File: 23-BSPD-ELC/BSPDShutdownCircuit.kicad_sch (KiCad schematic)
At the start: 15 parts, among them Q3 Q_NMOS_GSD-Device, Q4 Q_NMOS_GSD-Device, Q5 Q_PMOS_GDS, Q6 Q_PMOS_GDS

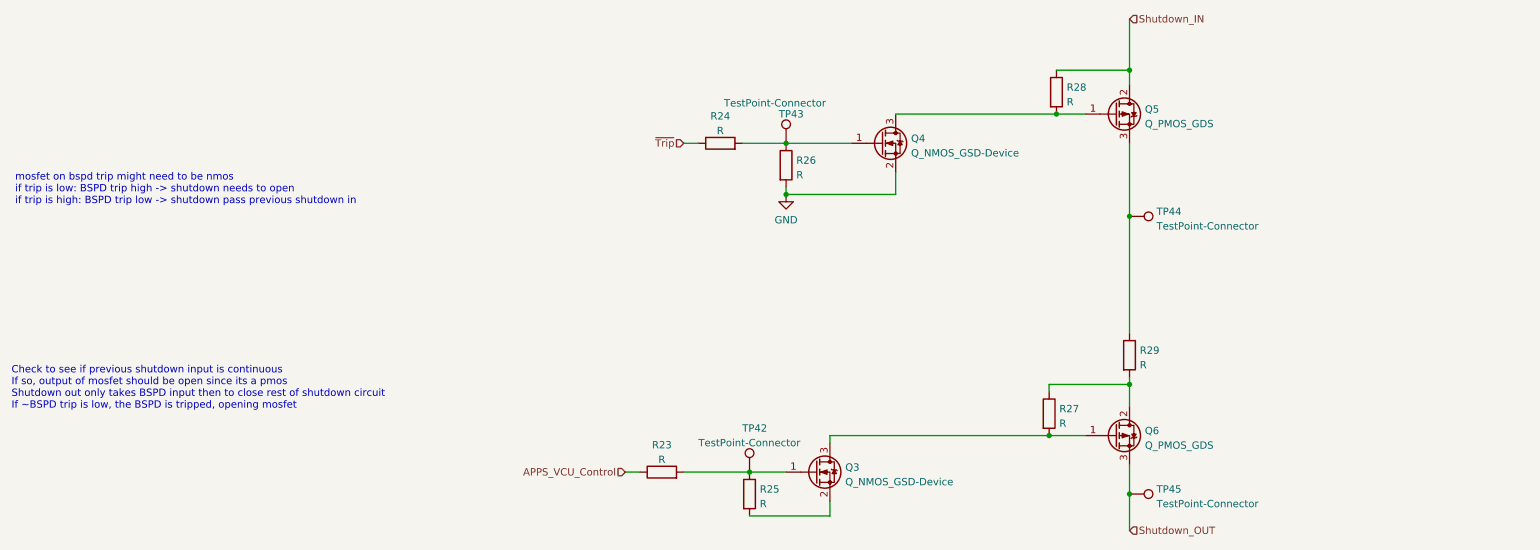
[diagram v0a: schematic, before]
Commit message: Revision changes and updates to some footprints
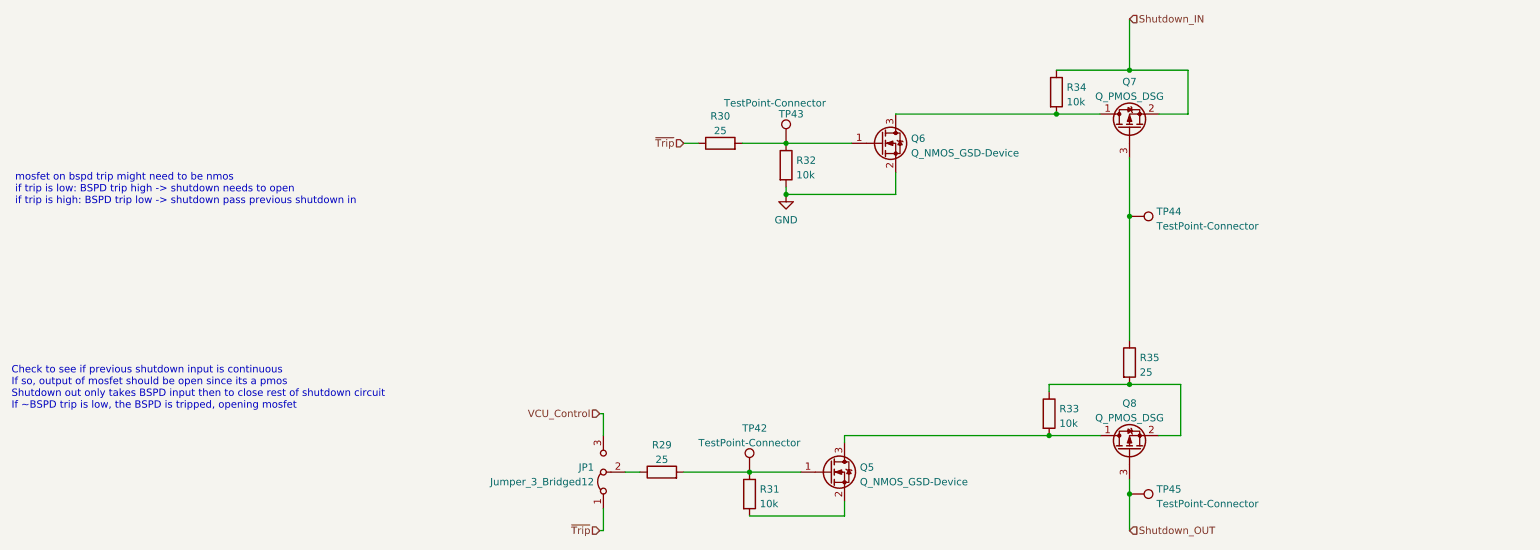
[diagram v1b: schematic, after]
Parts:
- removed Q3: Q_NMOS_GSD-Device, symbol 20-ELC-2-01-R1(Appetizer)-rescue:Q_NMOS_GSD-Device
- removed Q5, Q6: Q_PMOS_GDS, symbol Device:Q_PMOS_GDS
- added JP1: Jumper_3_Bridged12, symbol Jumper:Jumper_3_Bridged12
- added Q5: Q_NMOS_GSD-Device, symbol 20-ELC-2-01-R1(Appetizer)-rescue:Q_NMOS_GSD-Device
- added Q7, Q8: Q_PMOS_DSG, symbol Device:Q_PMOS_DSG
- R29: renamed from R23; value R -> 25
- R30: renamed from R24; value R -> 25
- R31: renamed from R25; value R -> 10k
- R32: renamed from R26; value R -> 10k
- R33: renamed from R27; value R -> 10k
- R34: renamed from R28; value R -> 10k
- R35: renamed from R29; value R -> 25
- renumbered Q4 to Q6
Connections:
- net Shutdown_IN: now also Q7.2 (S)
- net Shutdown_OUT: now also Q8.3 (G)
- net ~{Trip}: now also JP1.1 (A)
- net at Q6.3 (D), R34.2: now also Q7.1 (D)
- net at R35.1, TP44.1: now also Q7.3 (G)
- net at R33.1, R35.2: now also Q8.2 (S)
- net at R33.2: now also Q5.3 (D), Q8.1 (D)
- net at R29.2, R31.1, TP42.1: now also Q5.1 (G)
- net at R31.2: now also Q5.2 (S)
- net APPS_VCU_Control: no longer names the net of R29.1
- net APPS_VCU_Control: now also JP1.2 (C)
- new net VCU_Control: JP1.3 (B)
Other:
- moved on the sheet: R35

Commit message: Updated pcb layout; Watchdog on board still in progress
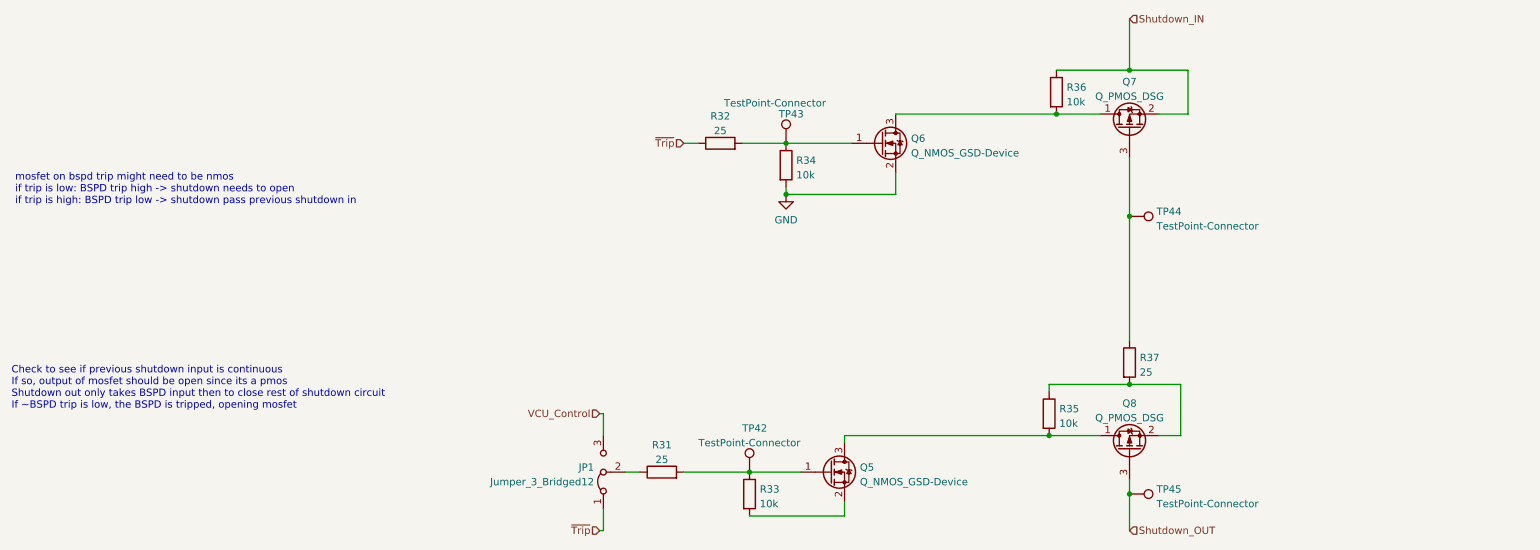
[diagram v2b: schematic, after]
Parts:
- JP1: footprint (none) -> Jumper:SolderJumper-3_P1.3mm_Bridged12_RoundedPad1.0x1.5mm
- Q5, Q6, Q7, Q8: footprint (none) -> Package_TO_SOT_SMD:TSOT-23
- renumbered R29 to R31, R30 to R32, R31 to R33, R32 to R34, R33 to R35, R34 to R36, R35 to R37
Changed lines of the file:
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@@
     (property "Reference" "Q7" (id 0) (at 231.14 38.8452 90))
     (property "Value" "Q_PMOS_DSG" (id 1) (at 231.14 41.3821 90))
-    (property "Footprint" "" (id 2) (at 228.6 41.91 0)
+    (property "Footprint" "Package_TO_SOT_SMD:TSOT-23" (id 2) (at 228.6 41.91 0)
       (effects (font (size 1.27 1.27)) hide)
     )
@@
   (symbol (lib_id "Device:R") (at 218.44 40.64 0) (unit 1)
     (in_bom yes) (on_board yes) (fields_autoplaced)
-    (property "Reference" "R34" (id 0) (at 220.218 39.8053 0)
+    (property "Reference" "R36" (id 0) (at 220.218 39.8053 0)
       (effects (font (size 1.27 1.27)) (justify left))
     )
@@
   (symbol (lib_id "Device:R") (at 217.17 96.52 0) (unit 1)
     (in_bom yes) (on_board yes) (fields_autoplaced)
-    (property "Reference" "R33" (id 0) (at 218.948 95.6853 0)
+    (property "Reference" "R35" (id 0) (at 218.948 95.6853 0)
       (effects (font (size 1.27 1.27)) (justify left))
     )
@@
   (symbol (lib_id "Device:R") (at 160.02 49.53 90) (unit 1)
     (in_bom yes) (on_board yes) (fields_autoplaced)
-    (property "Reference" "R30" (id 0) (at 160.02 44.8142 90))
+    (property "Reference" "R32" (id 0) (at 160.02 44.8142 90))
     (property "Value" "25" (id 1) (at 160.02 47.3511 90))
     (property "Footprint" "Resistor_SMD:R_0603_1608Metric_Pad0.98x0.95mm_HandSolder" (id 2) (at 160.02 51.308 90)
@@
   (symbol (lib_id "Device:R") (at 231.14 87.63 0) (unit 1)
     (in_bom yes) (on_board yes) (fields_autoplaced)
-    (property "Reference" "R35" (id 0) (at 232.918 86.7953 0)
+    (property "Reference" "R37" (id 0) (at 232.918 86.7953 0)
       (effects (font (size 1.27 1.27)) (justify left))
     )
@@
       (effects (font (size 1.27 1.27)) (justify left))
     )
-    (property "Footprint" "" (id 2) (at 193.04 46.99 0)
+    (property "Footprint" "Package_TO_SOT_SMD:TSOT-23" (id 2) (at 193.04 46.99 0)
       (effects (font (size 1.27 1.27)) hide)
     )
@@
     (property "Reference" "Q8" (id 0) (at 231.14 94.7252 90))
     (property "Value" "Q_PMOS_DSG" (id 1) (at 231.14 97.2621 90))
-    (property "Footprint" "" (id 2) (at 228.6 97.79 0)
+    (property "Footprint" "Package_TO_SOT_SMD:TSOT-23" (id 2) (at 228.6 97.79 0)
       (effects (font (size 1.27 1.27)) hide)
     )
@@
   (symbol (lib_id "Device:R") (at 171.45 53.34 0) (unit 1)
     (in_bom yes) (on_board yes) (fields_autoplaced)
-    (property "Reference" "R32" (id 0) (at 173.228 52.5053 0)
+    (property "Reference" "R34" (id 0) (at 173.228 52.5053 0)
       (effects (font (size 1.27 1.27)) (justify left))
     )
@@
       (effects (font (size 1.27 1.27)) (justify left))
     )
-    (property "Footprint" "" (id 2) (at 139.7 106.68 0)
+    (property "Footprint" "Jumper:SolderJumper-3_P1.3mm_Bridged12_RoundedPad1.0x1.5mm" (id 2) (at 139.7 106.68 0)
       (effects (font (size 1.27 1.27)) hide)
     )
@@
   (symbol (lib_id "Device:R") (at 165.1 110.49 0) (unit 1)
     (in_bom yes) (on_board yes) (fields_autoplaced)
-    (property "Reference" "R31" (id 0) (at 166.878 109.6553 0)
+    (property "Reference" "R33" (id 0) (at 166.878 109.6553 0)
       (effects (font (size 1.27 1.27)) (justify left))
     )
@@
   (symbol (lib_id "Device:R") (at 149.86 106.68 90) (unit 1)
     (in_bom yes) (on_board yes) (fields_autoplaced)
-    (property "Reference" "R29" (id 0) (at 149.86 101.9642 90))
+    (property "Reference" "R31" (id 0) (at 149.86 101.9642 90))
     (property "Value" "25" (id 1) (at 149.86 104.5011 90))
     (property "Footprint" "Resistor_SMD:R_0603_1608Metric_Pad0.98x0.95mm_HandSolder" (id 2) (at 149.86 108.458 90)
@@
       (effects (font (size 1.27 1.27)) (justify left))
     )
-    (property "Footprint" "" (id 2) (at 184.15 104.14 0)
-      (effects (font (size 1.27 1.27)) hide)
-    )
+    (property "Footprint" "Package_TO_SOT_SMD:TSOT-23" (id 2) (at 184.15 104.14 0)
+      (effects (font (size 1.27 1.27)) hide)
+    )

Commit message: BSPD layout
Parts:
- removed R37: 25, Resistor_SMD:R_0603_1608Metric_Pad0.98x0.95mm_HandSolder, symbol Device:R
- Q7, Q8: symbol Device:Q_PMOS_DSG -> Device:Q_PMOS_GSD
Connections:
- net Shutdown_IN: now also Q7.3 (D); no longer Q7.2 (S)
- net Shutdown_OUT: now also Q8.2 (S); no longer Q8.3 (G)
- net at TP44.1: now also Q7.2 (S), Q8.3 (D), R35.1; no longer Q7.3 (G)
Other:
- note added: "Change so gate of mosfet is towards source of nmos"
- moved on the sheet: Q7, Q8, TP44, TP45
